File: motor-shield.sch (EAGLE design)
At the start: 30 parts, among them IC1 24AA01P, K1 PIN20X2

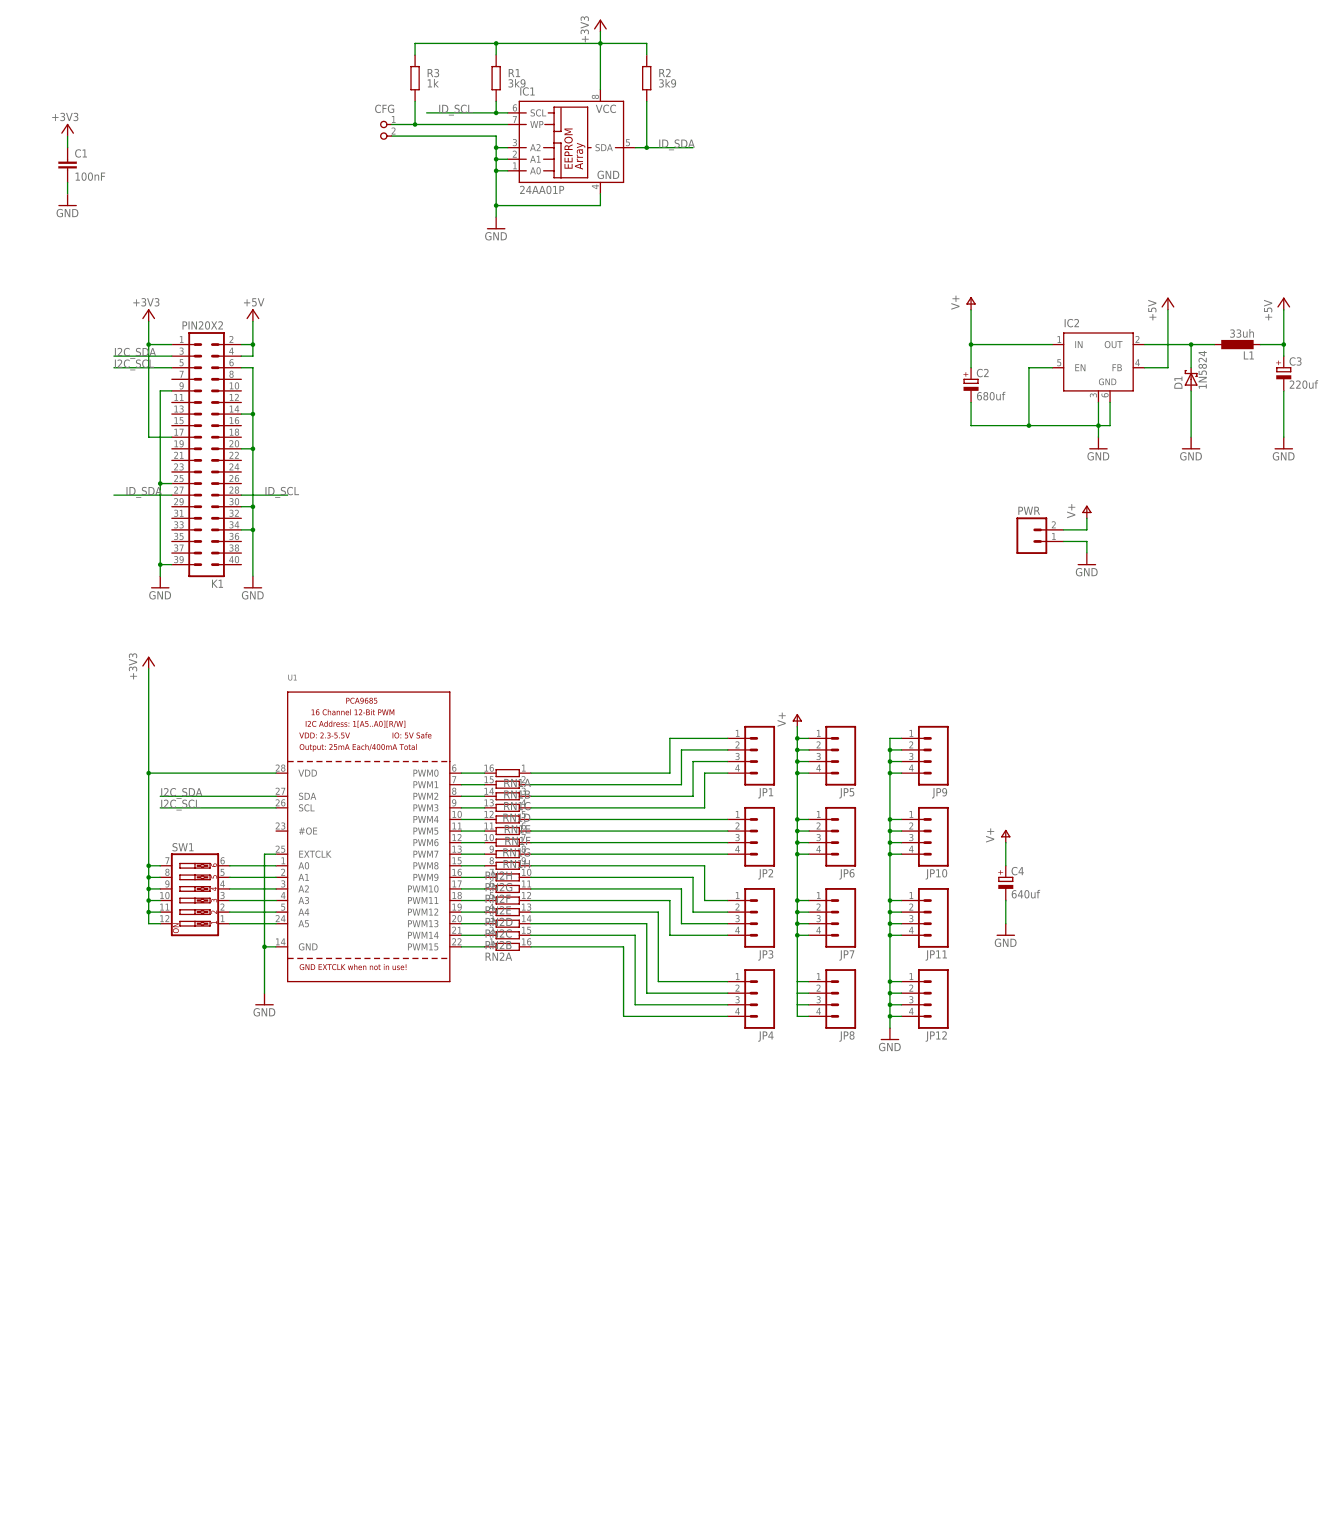
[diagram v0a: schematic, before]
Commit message: Complete, no air wires, passes DRC
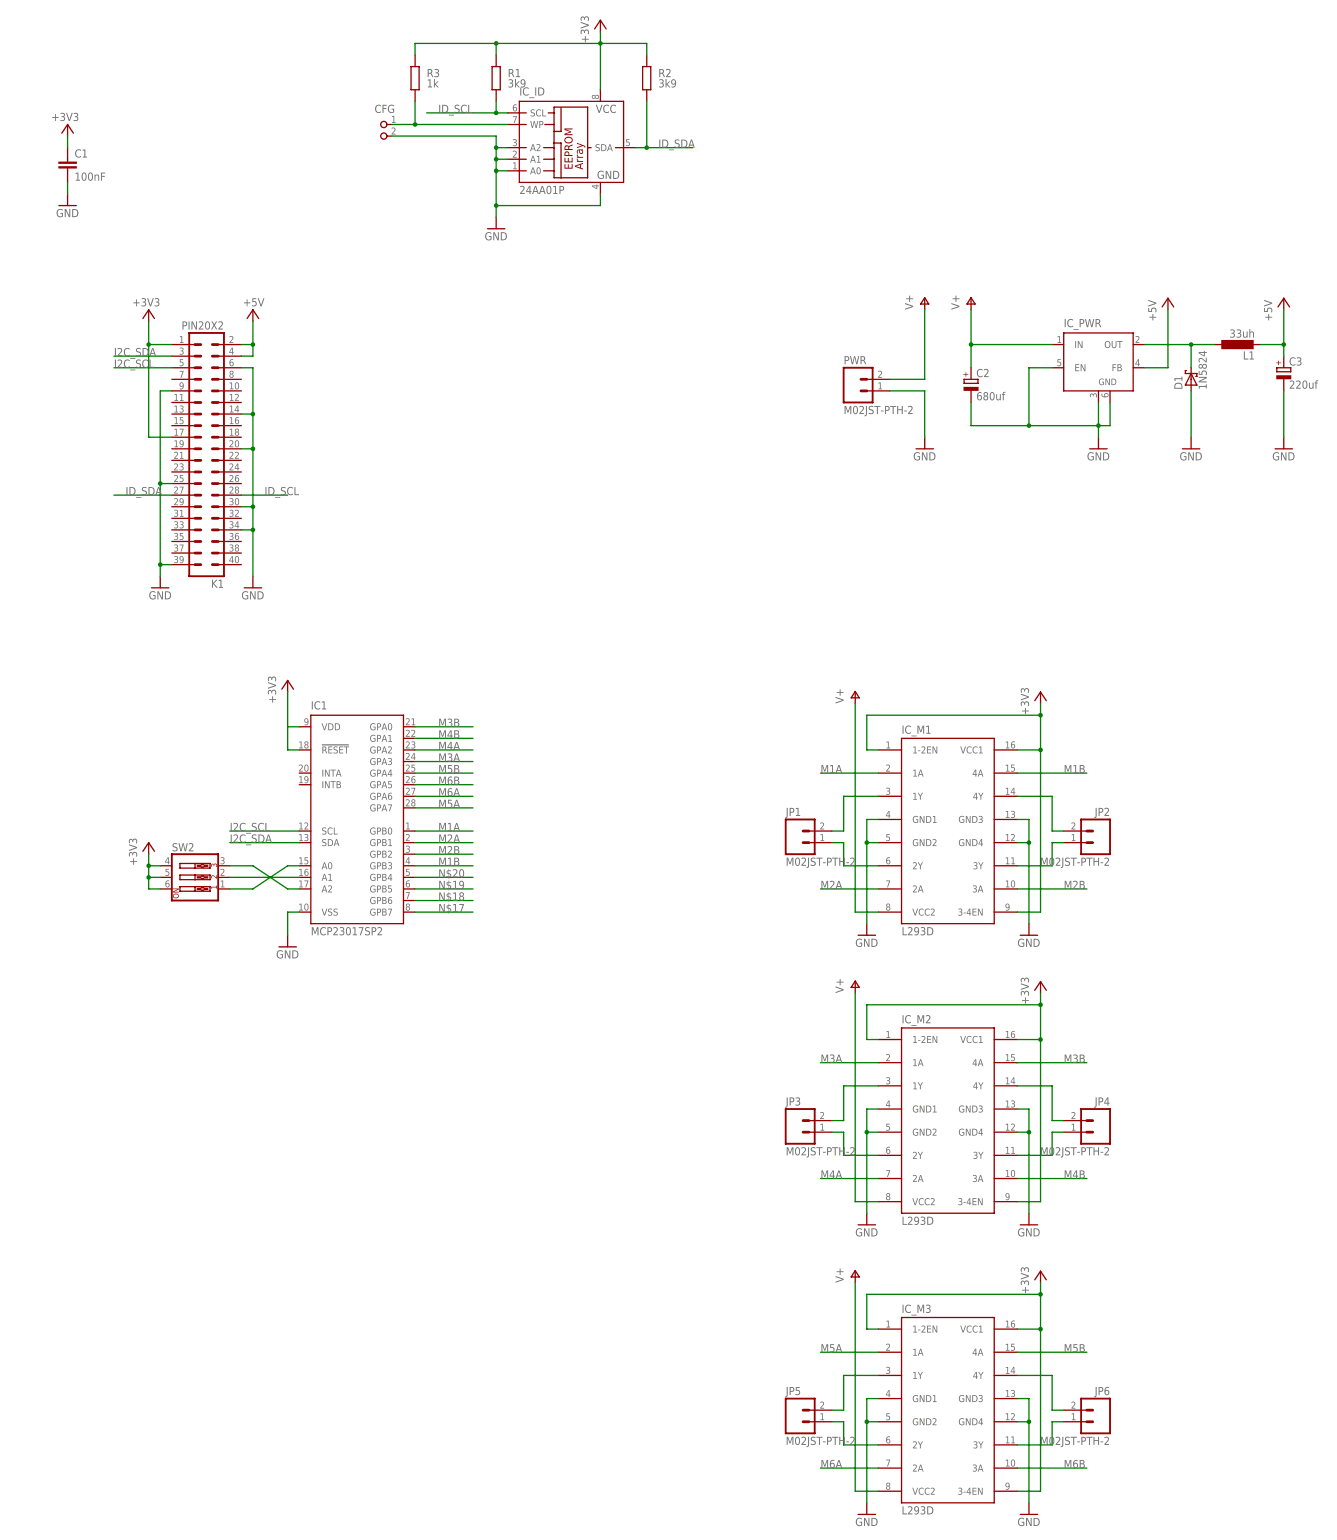
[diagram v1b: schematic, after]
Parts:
- removed C4: 640uf, rcl:CPOL-EUE2.5-6
- removed JP10, JP11, JP12, JP7, JP8, JP9: (no value), SparkFun-Connectors:M04LOCK
- removed RN1, RN2: (no value), resistor-dil:8R-N
- removed SW1: (no value), special:SW_DIP-6
- removed U1: (no value), adafruit:PCA9685
- added IC_ID: 24AA01P, microchip:24AA01P
- added IC_M1, IC_M2, IC_M3: L293D, st-microelectronics:L293D
- added SW2: (no value), special:SW_DIP-3
- IC1: value 24AA01P -> MCP23017SP2; device microchip:24AA01P -> adafruit:MCP23017SP2
- JP1, JP2, JP3, JP4, JP5, JP6: value (none) -> M02JST-PTH-2; device SparkFun-Connectors:M04LOCK -> SparkFun-Connectors:M02JST-PTH-2
- renumbered IC2 to IC_PWR
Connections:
- removed net N$21: JP4.3, RN2B.2
- removed net N$22: JP4.4, RN2A.2
- removed net N$23: RN2A.1, U1.PWM15
- removed net N$24: RN2B.1, U1.PWM14
- removed net N$25: RN2C.1, U1.PWM13
- removed net N$26: RN2D.1, U1.PWM12
- removed net N$27: RN2E.1, U1.PWM11
- removed net N$28: RN2F.1, U1.PWM10
- removed net N$29: RN1G.2, U1.PWM6
- removed net N$30: RN1F.2, U1.PWM5
- removed net N$31: RN1E.2, U1.PWM4
- removed net N$32: RN1D.2, U1.PWM3
- removed net N$33: RN1C.2, U1.PWM2
- removed net N$34: RN1B.2, U1.PWM1
- removed net N$35: RN1A.2, U1.PWM0
- removed net N$36: JP2.1, RN1E.1
- removed net N$37: JP2.4, RN1H.1
- removed net N$38: JP2.3, RN1G.1
- removed net N$39: JP2.2, RN1F.1
- new net M1A: IC1.GPB0, IC_M1.1A
- new net M1B: IC1.GPB3, IC_M1.4A
- new net M2A: IC1.GPB1, IC_M1.2A
- new net M2B: IC1.GPB2, IC_M1.3A
- new net M3A: IC1.GPA3, IC_M2.1A
- new net M3B: IC1.GPA0, IC_M2.4A
- new net M4A: IC1.GPA2, IC_M2.2A
- new net M4B: IC1.GPA1, IC_M2.3A
- new net M5A: IC1.GPA7, IC_M3.1A
- new net M5B: IC1.GPA4, IC_M3.4A
- new net M6A: IC1.GPA6, IC_M3.2A
- new net M6B: IC1.GPA5, IC_M3.3A
- net +3V3: now also IC1.!RESET, IC1.VDD, IC_ID.VCC, IC_M1.1-2EN, IC_M1.3-4EN, IC_M1.VCC1, IC_M2.1-2EN, IC_M2.3-4EN, IC_M2.VCC1, IC_M3.1-2EN, IC_M3.3-4EN, IC_M3.VCC1, SW2.4, SW2.5, SW2.6; no longer IC1.VCC, SW1.10, SW1.11, SW1.12, SW1.7, SW1.8, SW1.9, U1.VDD
- net GND: now also IC1.VSS, IC_ID.A0, IC_ID.A1, IC_ID.A2, IC_ID.GND, IC_M1.GND1, IC_M1.GND2, IC_M1.GND3, IC_M1.GND4, IC_M2.GND1, IC_M2.GND2, IC_M2.GND3, IC_M2.GND4, IC_M3.GND1, IC_M3.GND2, IC_M3.GND3, IC_M3.GND4; no longer C4.-, IC1.A0, IC1.A1, IC1.A2, IC1.GND, JP10.1, JP10.2, JP10.3, JP10.4, JP11.1, JP11.2, JP11.3, JP11.4, JP12.1, JP12.2, JP12.3, JP12.4, JP9.1, JP9.2, JP9.3, JP9.4, U1.EXTCLK, U1.GND
- net I2C_SCL: now also IC1.SCL; no longer U1.SCL
- net I2C_SDA: now also IC1.SDA; no longer U1.SDA
- net ID_SCL: now also IC_ID.SCL; no longer IC1.SCL
- net ID_SDA: now also IC_ID.SDA; no longer IC1.SDA
- net N$1: now also IC1.A2, SW2.3; no longer RN2G.1, U1.PWM9
- net N$10: now also IC_M1.1Y, JP1.2; no longer JP3.2, RN2G.2
- net N$11: now also IC_M2.2Y, JP3.1; no longer SW1.1, U1.A5
- net N$12: now also IC_M2.1Y, JP3.2; no longer SW1.2, U1.A4
- net N$13: now also IC_M3.3Y, JP6.1; no longer SW1.3, U1.A3
- net N$14: now also IC_M3.4Y, JP6.2; no longer SW1.4, U1.A2
- net N$15: now also IC_M3.2Y, JP5.1; no longer SW1.5, U1.A1
- net N$16: now also IC_M3.1Y, JP5.2; no longer SW1.6, U1.A0
- net N$17: now also IC1.GPB7; no longer JP3.3, RN2F.2
- net N$18: now also IC1.GPB6; no longer JP3.4, RN2E.2
- net N$19: now also IC1.GPB5; no longer JP4.1, RN2D.2
- net N$2: now also IC1.A1, SW2.2; no longer RN2H.1, U1.PWM8
- net N$20: now also IC1.GPB4; no longer JP4.2, RN2C.2
- net N$3: now also IC1.A0, SW2.1; no longer RN1H.2, U1.PWM7
- net N$4: now also IC_ID.WP; no longer IC1.WP
- net N$5: now also IC_M2.3Y, JP4.1; no longer JP1.4, RN1D.1
- net N$6: now also IC_M2.4Y, JP4.2; no longer JP1.3, RN1C.1
- net N$7: now also IC_M1.3Y, JP2.1; no longer JP1.2, RN1B.1
- net N$8: now also IC_M1.4Y, JP2.2; no longer JP1.1, RN1A.1
- net N$9: now also IC_M1.2Y, JP1.1; no longer JP3.1, RN2H.2
- net V+: now also IC_M1.VCC2, IC_M2.VCC2, IC_M3.VCC2; no longer C4.+, JP5.1, JP5.2, JP5.3, JP5.4, JP6.1, JP6.2, JP6.3, JP6.4, JP7.1, JP7.2, JP7.3, JP7.4, JP8.1, JP8.2, JP8.3, JP8.4
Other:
- moved on the sheet: PWR

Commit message: Rebuilt to match servo shield
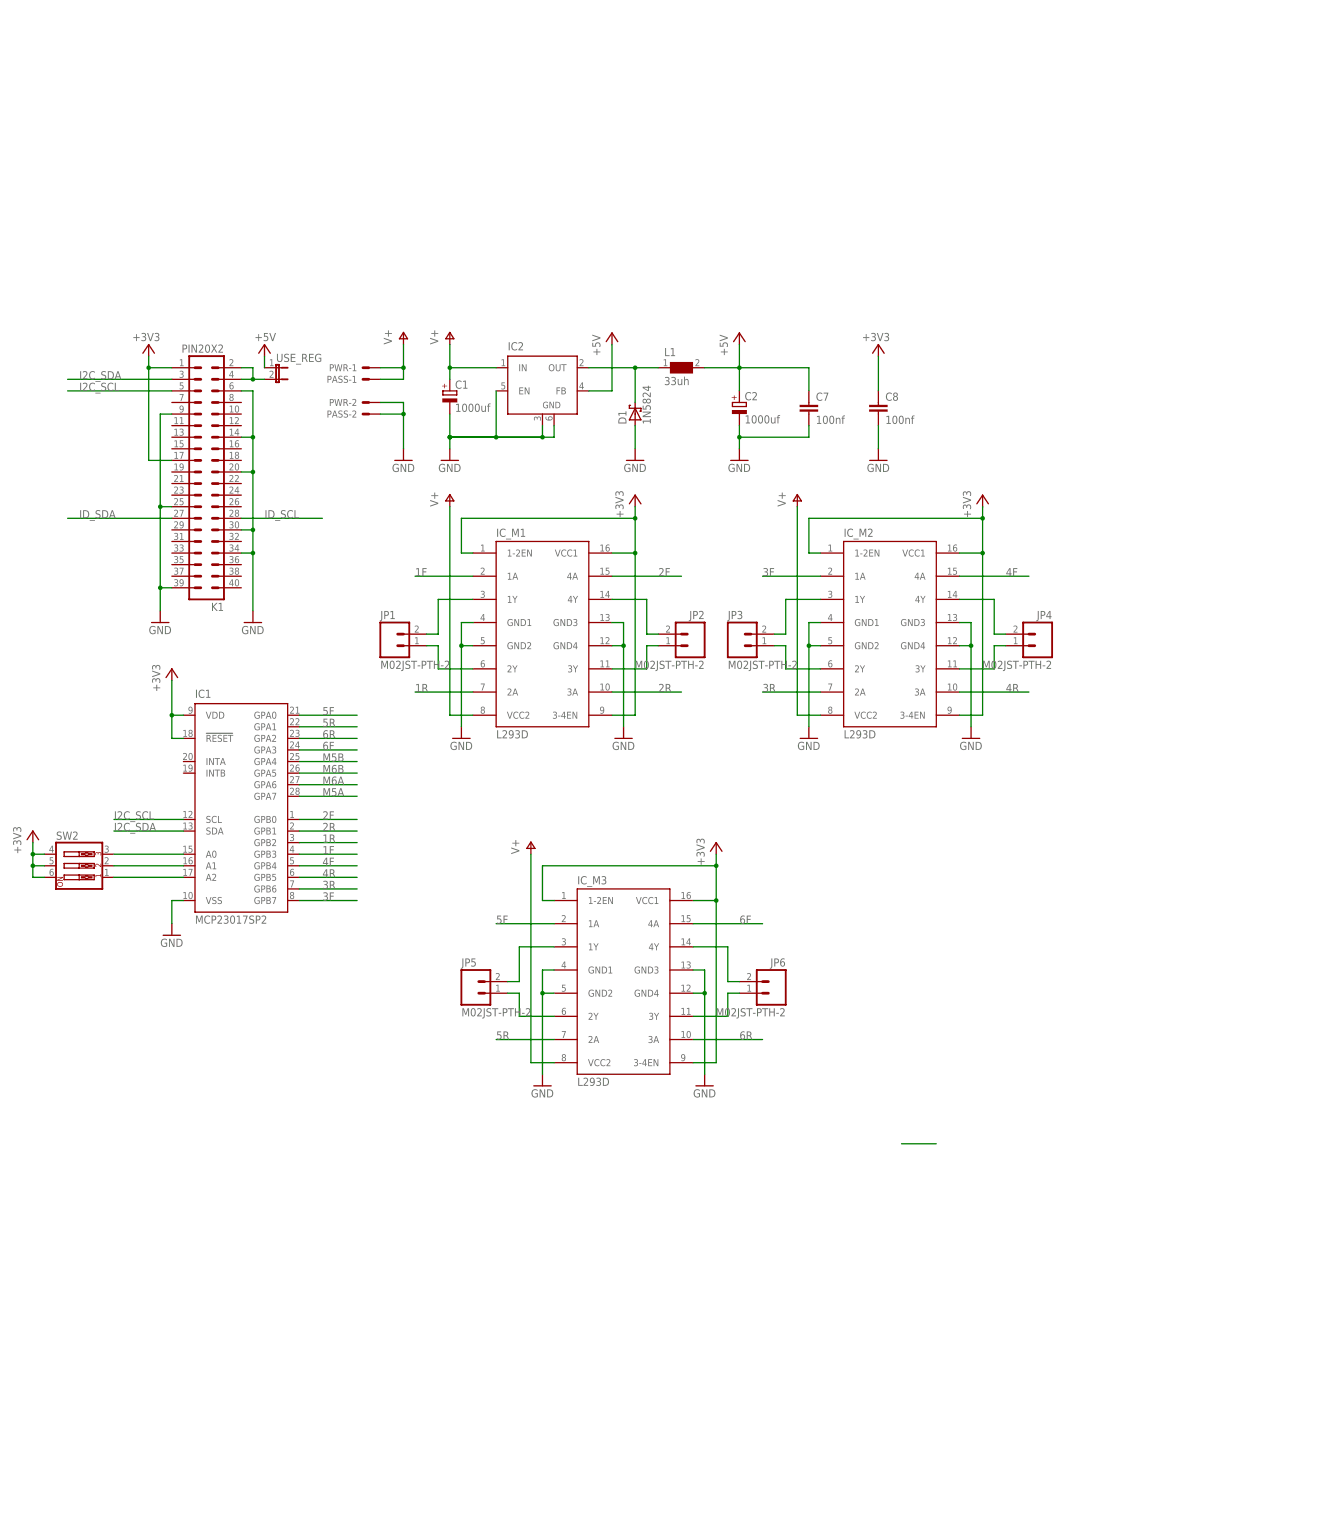
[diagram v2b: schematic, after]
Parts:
- removed C3: 220uf, rcl:CPOL-EUE2.5-6
- removed CFG: (no value), FLYFISH:PIN2_100
- removed IC_ID: 24AA01P, microchip:24AA01P
- removed IC_PWR: (no value), linear:LM2596S
- removed R1, R2: 3k9, rcl:R-EU_0204/7
- removed R3: 1k, rcl:R-EU_0204/7
- added C7, C8: 100nf, rcl:C-EU025-030X050
- added IC2: (no value), linear:LM2596S
- added PASS: 22-05-7028-02, con-molex:22-05-7028-02
- added USE_REG: (no value), jumper:JP1E
- C1: value 100nF -> 1000uf; device rcl:C-EU025-030X050 -> rcl:CPOL-EUE2.5-6; DIELECTRIC X7R -> (none)
- C2: value 680uf -> 1000uf; device rcl:CPOL-EUE2.5-6 -> rcl:CPOL-EUE2.5-7
- L1: device rcl:L-EU0207/10 -> WE-PD:WE-PD-744770133_1260/1245/1280/1210
- PWR: value M02JST-PTH-2 -> 22-05-7028-02; device SparkFun-Connectors:M02JST-PTH-2 -> con-molex:22-05-7028-02
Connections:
- removed net M1A: IC1.GPB0, IC_M1.1A
- removed net M1B: IC1.GPB3, IC_M1.4A
- removed net M2A: IC1.GPB1, IC_M1.2A
- removed net M2B: IC1.GPB2, IC_M1.3A
- removed net M3A: IC1.GPA3, IC_M2.1A
- removed net M3B: IC1.GPA0, IC_M2.4A
- removed net M4A: IC1.GPA2, IC_M2.2A
- removed net M4B: IC1.GPA1, IC_M2.3A
- removed net N$1 (its old number): IC1.A2, SW2.3
- removed net N$17: IC1.GPB7
- removed net N$18: IC1.GPB6
- removed net N$19: IC1.GPB5
- removed net N$20: IC1.GPB4
- removed net N$3 (its old number): IC1.A0, SW2.1
- removed net N$4: CFG.1, IC_ID.WP, R3.1
- removed net N$40: D1.C, IC_PWR.OUT, L1.1
- new net 1F: IC1.GPB3, IC_M1.1A
- new net 1R: IC1.GPB2, IC_M1.2A
- new net 2F: IC1.GPB0, IC_M1.4A
- new net 2R: IC1.GPB1, IC_M1.3A
- new net 3F: IC1.GPB7, IC_M2.1A
- new net 3R: IC1.GPB6, IC_M2.2A
- new net 4F: IC1.GPB4, IC_M2.4A
- new net 4R: IC1.GPB5, IC_M2.3A
- new net 5F: IC1.GPA0, IC_M3.1A
- new net 5R: IC1.GPA1, IC_M3.2A
- new net 6F: IC1.GPA3, IC_M3.4A
- new net 6R: IC1.GPA2, IC_M3.3A
- new net N$16: K1.2, K1.4, USE_REG.2
- new net N$2: IC1.A0, SW2.3
- new net N$23: IC1.A2, SW2.1
- new net VOUT: D1.C, IC2.OUT, L1.1
- net +3V3: now also C8.1; no longer C1.1, IC_ID.VCC, R1.2, R2.2, R3.2
- net +5V: now also C2.+, C7.1, IC2.FB, USE_REG.1; no longer C3.+, IC_PWR.FB, K1.2, K1.4
- net GND: now also C1.-, C7.2, C8.2, IC2.EN, IC2.GND, IC2.GND@1, PASS-2.S, PWR-2.S; no longer C1.2, C3.-, CFG.2, IC_ID.A0, IC_ID.A1, IC_ID.A2, IC_ID.GND, IC_PWR.EN, IC_PWR.GND, IC_PWR.GND@1, PWR.1
- net ID_SCL: no longer IC_ID.SCL, R1.1
- net ID_SDA: no longer IC_ID.SDA, R2.1
- net M5A: no longer IC_M3.1A
- net M5B: no longer IC_M3.4A
- net M6A: no longer IC_M3.2A
- net M6B: no longer IC_M3.3A
- net V+: now also C1.+, IC2.IN, PASS-1.S, PWR-1.S; no longer C2.+, IC_PWR.IN, PWR.2
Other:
- moved on the sheet: C2, D1, IC1, IC_M1, IC_M2, IC_M3, JP1, JP2, JP3, JP4, JP5, JP6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
